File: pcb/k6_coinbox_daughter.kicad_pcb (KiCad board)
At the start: 2 copper layers, 45 x 35 mm, 17 parts, among them J1 COIN, J2 BTN_A, J3 BTN_B, J4 TO_ESP32, U1 PC817, U2 PC817, U3 PC817

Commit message: feat: update daughter board J4 to 6-pin header (separate +3V3 and +5V)
- J4 now has 6 pins matching carrier board J_COIN: COIN, A, B, 3V3, GND, 5V
- VCC_3V3 powers pull-up resistors R4/R5/R6 (3.3V logic for ESP32)
- VCC_5V available for optocoupler LED drive (input side)
- Pin order enables straight ribbon cable connection to carrier board
- Updated documentation and regenerated PCB file

Co-Authored-By: Devin AI <158243242+devin-ai-integration[bot]@users.noreply.github.com>
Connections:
- J4 pad 1: VCC -> COIN_SENSE
- J4 pad 2: COIN_SENSE -> BTN_A
- J4 pad 3: BTN_A -> BTN_B
- J4 pad 4: BTN_B -> VCC_3V3
- R4 pad 1: VCC -> VCC_3V3
- R5 pad 1: VCC -> VCC_3V3
- R6 pad 1: VCC -> VCC_3V3
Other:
- board text added: "3V3"
- board text added: "5V"
- board text removed: "VCC"
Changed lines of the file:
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@@
     )
     (net 0 "")
-(net 1 "VCC")
+(net 1 "VCC_3V3")
 (net 2 "GND")
 (net 3 "COIN_SENSE")
@@
 (net 13 "OPTO2_CA")
 (net 14 "OPTO3_CA")
+(net 15 "VCC_5V")
     (gr_line (start 131.5 90.0) (end 173.5 90.0) (stroke (width 0.05) (type default)) (layer "Edge.Cuts"))
 (gr_line (start 131.5 125.0) (end 173.5 125.0) (stroke (width 0.05) (type default)) (layer "Edge.Cuts"))
@@
   (fp_line (start -2.810 -1.0) (end 2.810 -1.0) (stroke (width 0.12) (type default)) (layer "F.SilkS"))
   (fp_line (start -2.810 1.0) (end 2.810 1.0) (stroke (width 0.12) (type default)) (layer "F.SilkS"))
-(pad "1" thru_hole circle (at -3.810 0.000) (size 1.7 1.7) (drill 1.0) (layers "*.Cu" "*.Mask") (net 1 "VCC"))
+(pad "1" thru_hole circle (at -3.810 0.000) (size 1.7 1.7) (drill 1.0) (layers "*.Cu" "*.Mask") (net 1 "VCC_3V3"))
 (pad "2" thru_hole circle (at 3.810 0.000) (size 1.7 1.7) (drill 1.0) (layers "*.Cu" "*.Mask") (net 3 "COIN_SENSE"))
 )
@@
   (fp_line (start -2.810 -1.0) (end 2.810 -1.0) (stroke (width 0.12) (type default)) (layer "F.SilkS"))
   (fp_line (start -2.810 1.0) (end 2.810 1.0) (stroke (width 0.12) (type default)) (layer "F.SilkS"))
-(pad "1" thru_hole circle (at -3.810 0.000) (size 1.7 1.7) (drill 1.0) (layers "*.Cu" "*.Mask") (net 1 "VCC"))
+(pad "1" thru_hole circle (at -3.810 0.000) (size 1.7 1.7) (drill 1.0) (layers "*.Cu" "*.Mask") (net 1 "VCC_3V3"))
 (pad "2" thru_hole circle (at 3.810 0.000) (size 1.7 1.7) (drill 1.0) (layers "*.Cu" "*.Mask") (net 4 "BTN_A"))
 )
@@
   (fp_line (start -2.810 -1.0) (end 2.810 -1.0) (stroke (width 0.12) (type default)) (layer "F.SilkS"))
   (fp_line (start -2.810 1.0) (end 2.810 1.0) (stroke (width 0.12) (type default)) (layer "F.SilkS"))
-(pad "1" thru_hole circle (at -3.810 0.000) (size 1.7 1.7) (drill 1.0) (layers "*.Cu" "*.Mask") (net 1 "VCC"))
+(pad "1" thru_hole circle (at -3.810 0.000) (size 1.7 1.7) (drill 1.0) (layers "*.Cu" "*.Mask") (net 1 "VCC_3V3"))
 (pad "2" thru_hole circle (at 3.810 0.000) (size 1.7 1.7) (drill 1.0) (layers "*.Cu" "*.Mask") (net 5 "BTN_B"))
 )
@@
   (effects (font (size 0.8 0.8) (thickness 0.12)))
 )
-  (fp_rect (start -1.5 -6.850) (end 1.5 6.850) (stroke (width 0.05) (type default)) (fill none) (layer "F.CrtYd"))
-(pad "1" thru_hole circle (at 0.000 -5.080) (size 1.7 1.7) (drill 1.0) (layers "*.Cu" "*.Mask") (net 1 "VCC"))
-(pad "2" thru_hole circle (at 0.000 -2.540) (size 1.7 1.7) (drill 1.0) (layers "*.Cu" "*.Mask") (net 3 "COIN_SENSE"))
-(pad "3" thru_hole circle (at 0.000 0.000) (size 1.7 1.7) (drill 1.0) (layers "*.Cu" "*.Mask") (net 4 "BTN_A"))
-(pad "4" thru_hole circle (at 0.000 2.540) (size 1.7 1.7) (drill 1.0) (layers "*.Cu" "*.Mask") (net 5 "BTN_B"))
-(pad "5" thru_hole circle (at 0.000 5.080) (size 1.7 1.7) (drill 1.0) (layers "*.Cu" "*.Mask") (net 2 "GND"))
+  (fp_rect (start -1.5 -8.120) (end 1.5 8.120) (stroke (width 0.05) (type default)) (fill none) (layer "F.CrtYd"))
+(pad "1" thru_hole circle (at 0.000 -6.350) (size 1.7 1.7) (drill 1.0) (layers "*.Cu" "*.Mask") (net 3 "COIN_SENSE"))
+(pad "2" thru_hole circle (at 0.000 -3.810) (size 1.7 1.7) (drill 1.0) (layers "*.Cu" "*.Mask") (net 4 "BTN_A"))
+(pad "3" thru_hole circle (at 0.000 -1.270) (size 1.7 1.7) (drill 1.0) (layers "*.Cu" "*.Mask") (net 5 "BTN_B"))
+(pad "4" thru_hole circle (at 0.000 1.270) (size 1.7 1.7) (drill 1.0) (layers "*.Cu" "*.Mask") (net 1 "VCC_3V3"))
+(pad "5" thru_hole circle (at 0.000 3.810) (size 1.7 1.7) (drill 1.0) (layers "*.Cu" "*.Mask") (net 2 "GND"))
+(pad "6" thru_hole circle (at 0.000 6.350) (size 1.7 1.7) (drill 1.0) (layers "*.Cu" "*.Mask") (net 15 "VCC_5V"))
 )
 (footprint "K6_COINBOX:MH1" (layer "F.Cu")
@@
   (effects (font (size 0.8 0.8) (thickness 0.12)))
 )
-(gr_text "VCC" (at 172.000 98.500) (layer "F.SilkS")
-  (effects (font (size 0.8 0.8) (thickness 0.12)))
-)
-(gr_text "COIN" (at 172.000 101.000) (layer "F.SilkS")
-  (effects (font (size 0.8 0.8) (thickness 0.12)))
-)
-(gr_text "A" (at 172.000 103.500) (layer "F.SilkS")
-  (effects (font (size 0.8 0.8) (thickness 0.12)))
-)
-(gr_text "B" (at 172.000 106.000) (layer "F.SilkS")
-  (effects (font (size 0.8 0.8) (thickness 0.12)))
-)
-(gr_text "GND" (at 172.000 108.500) (layer "F.SilkS")
-  (effects (font (size 0.8 0.8) (thickness 0.12)))
-)
+(gr_text "COIN" (at 172.000 98.000) (layer "F.SilkS")
+  (effects (font (size 0.8 0.8) (thickness 0.12)))
+)
+(gr_text "A" (at 172.000 100.500) (layer "F.SilkS")
+  (effects (font (size 0.8 0.8) (thickness 0.12)))
+)
+(gr_text "B" (at 172.000 103.000) (layer "F.SilkS")
+  (effects (font (size 0.8 0.8) (thickness 0.12)))
+)
+(gr_text "3V3" (at 172.000 105.500) (layer "F.SilkS")
+  (effects (font (size 0.8 0.8) (thickness 0.12)))
+)
+(gr_text "GND" (at 172.000 108.000) (layer "F.SilkS")
+  (effects (font (size 0.8 0.8) (thickness 0.12)))
+)
+(gr_text "5V" (at 172.000 110.500) (layer "F.SilkS")
+  (effects (font (size 0.8 0.8) (thickness 0.12)))
+)

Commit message: feat: integrate VCC_5V into daughter board input circuit
- VCC_5V now drives pin 1 of each screw terminal (C+/A+/B+)
- A+B box contacts are dry switches bridging pin 1 to pin 2
- When switch closes: 5V -> R(470R) -> opto LED -> GND = 8mA
- Opto LED cathodes now connected to GND (were floating to return pin)
- No external voltage source needed for the A+B box contacts
- Updated circuit diagram and wiring documentation

Co-Authored-By: Devin AI <158243242+devin-ai-integration[bot]@users.noreply.github.com>
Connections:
- J1 pad 1: COIN_IN_A -> VCC_5V
- J2 pad 1: BTNA_IN_A -> VCC_5V
- J3 pad 1: BTNB_IN_A -> VCC_5V
- R1 pad 1: COIN_IN_A -> COIN_IN_B
- R2 pad 1: BTNA_IN_A -> BTNA_IN_B
- R3 pad 1: BTNB_IN_A -> BTNB_IN_B
- U1 pad 2: COIN_IN_B -> GND
- U2 pad 2: BTNA_IN_B -> GND
- U3 pad 2: BTNB_IN_B -> GND
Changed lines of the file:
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@@
   (effects (font (size 0.8 0.8) (thickness 0.12)))
 )
-(pad "1" thru_hole circle (at -2.540 0.000) (size 2.5 2.5) (drill 1.3) (layers "*.Cu" "*.Mask") (net 6 "COIN_IN_A"))
+(pad "1" thru_hole circle (at -2.540 0.000) (size 2.5 2.5) (drill 1.3) (layers "*.Cu" "*.Mask") (net 15 "VCC_5V"))
 (pad "2" thru_hole circle (at 2.540 0.000) (size 2.5 2.5) (drill 1.3) (layers "*.Cu" "*.Mask") (net 7 "COIN_IN_B"))
 )
@@
   (effects (font (size 0.8 0.8) (thickness 0.12)))
 )
-(pad "1" thru_hole circle (at -2.540 0.000) (size 2.5 2.5) (drill 1.3) (layers "*.Cu" "*.Mask") (net 8 "BTNA_IN_A"))
+(pad "1" thru_hole circle (at -2.540 0.000) (size 2.5 2.5) (drill 1.3) (layers "*.Cu" "*.Mask") (net 15 "VCC_5V"))
 (pad "2" thru_hole circle (at 2.540 0.000) (size 2.5 2.5) (drill 1.3) (layers "*.Cu" "*.Mask") (net 9 "BTNA_IN_B"))
 )
@@
   (effects (font (size 0.8 0.8) (thickness 0.12)))
 )
-(pad "1" thru_hole circle (at -2.540 0.000) (size 2.5 2.5) (drill 1.3) (layers "*.Cu" "*.Mask") (net 10 "BTNB_IN_A"))
+(pad "1" thru_hole circle (at -2.540 0.000) (size 2.5 2.5) (drill 1.3) (layers "*.Cu" "*.Mask") (net 15 "VCC_5V"))
 (pad "2" thru_hole circle (at 2.540 0.000) (size 2.5 2.5) (drill 1.3) (layers "*.Cu" "*.Mask") (net 11 "BTNB_IN_B"))
 )
@@
   (fp_line (start -2.810 -1.0) (end 2.810 -1.0) (stroke (width 0.12) (type default)) (layer "F.SilkS"))
   (fp_line (start -2.810 1.0) (end 2.810 1.0) (stroke (width 0.12) (type default)) (layer "F.SilkS"))
-(pad "1" thru_hole circle (at -3.810 0.000) (size 1.7 1.7) (drill 1.0) (layers "*.Cu" "*.Mask") (net 6 "COIN_IN_A"))
+(pad "1" thru_hole circle (at -3.810 0.000) (size 1.7 1.7) (drill 1.0) (layers "*.Cu" "*.Mask") (net 7 "COIN_IN_B"))
 (pad "2" thru_hole circle (at 3.810 0.000) (size 1.7 1.7) (drill 1.0) (layers "*.Cu" "*.Mask") (net 12 "OPTO1_CA"))
 )
@@
   (fp_line (start -2.810 -1.0) (end 2.810 -1.0) (stroke (width 0.12) (type default)) (layer "F.SilkS"))
   (fp_line (start -2.810 1.0) (end 2.810 1.0) (stroke (width 0.12) (type default)) (layer "F.SilkS"))
-(pad "1" thru_hole circle (at -3.810 0.000) (size 1.7 1.7) (drill 1.0) (layers "*.Cu" "*.Mask") (net 8 "BTNA_IN_A"))
+(pad "1" thru_hole circle (at -3.810 0.000) (size 1.7 1.7) (drill 1.0) (layers "*.Cu" "*.Mask") (net 9 "BTNA_IN_B"))
 (pad "2" thru_hole circle (at 3.810 0.000) (size 1.7 1.7) (drill 1.0) (layers "*.Cu" "*.Mask") (net 13 "OPTO2_CA"))
 )
@@
   (fp_line (start -2.810 -1.0) (end 2.810 -1.0) (stroke (width 0.12) (type default)) (layer "F.SilkS"))
   (fp_line (start -2.810 1.0) (end 2.810 1.0) (stroke (width 0.12) (type default)) (layer "F.SilkS"))
-(pad "1" thru_hole circle (at -3.810 0.000) (size 1.7 1.7) (drill 1.0) (layers "*.Cu" "*.Mask") (net 10 "BTNB_IN_A"))
+(pad "1" thru_hole circle (at -3.810 0.000) (size 1.7 1.7) (drill 1.0) (layers "*.Cu" "*.Mask") (net 11 "BTNB_IN_B"))
 (pad "2" thru_hole circle (at 3.810 0.000) (size 1.7 1.7) (drill 1.0) (layers "*.Cu" "*.Mask") (net 14 "OPTO3_CA"))
 )
@@
   (fp_circle (center -4.310 -1.270) (end -4.010 -1.270) (stroke (width 0.12) (type default)) (fill solid) (layer "F.SilkS"))
 (pad "1" thru_hole circle (at -3.810 -1.270) (size 1.6 1.6) (drill 0.8) (layers "*.Cu" "*.Mask") (net 12 "OPTO1_CA"))
-(pad "2" thru_hole circle (at -3.810 1.270) (size 1.6 1.6) (drill 0.8) (layers "*.Cu" "*.Mask") (net 7 "COIN_IN_B"))
+(pad "2" thru_hole circle (at -3.810 1.270) (size 1.6 1.6) (drill 0.8) (layers "*.Cu" "*.Mask") (net 2 "GND"))
 (pad "4" thru_hole circle (at 3.810 -1.270) (size 1.6 1.6) (drill 0.8) (layers "*.Cu" "*.Mask") (net 3 "COIN_SENSE"))
 (pad "3" thru_hole circle (at 3.810 1.270) (size 1.6 1.6) (drill 0.8) (layers "*.Cu" "*.Mask") (net 2 "GND"))
@@
   (fp_circle (center -4.310 -1.270) (end -4.010 -1.270) (stroke (width 0.12) (type default)) (fill solid) (layer "F.SilkS"))
 (pad "1" thru_hole circle (at -3.810 -1.270) (size 1.6 1.6) (drill 0.8) (layers "*.Cu" "*.Mask") (net 13 "OPTO2_CA"))
-(pad "2" thru_hole circle (at -3.810 1.270) (size 1.6 1.6) (drill 0.8) (layers "*.Cu" "*.Mask") (net 9 "BTNA_IN_B"))
+(pad "2" thru_hole circle (at -3.810 1.270) (size 1.6 1.6) (drill 0.8) (layers "*.Cu" "*.Mask") (net 2 "GND"))
 (pad "4" thru_hole circle (at 3.810 -1.270) (size 1.6 1.6) (drill 0.8) (layers "*.Cu" "*.Mask") (net 4 "BTN_A"))
 (pad "3" thru_hole circle (at 3.810 1.270) (size 1.6 1.6) (drill 0.8) (layers "*.Cu" "*.Mask") (net 2 "GND"))
@@
   (fp_circle (center -4.310 -1.270) (end -4.010 -1.270) (stroke (width 0.12) (type default)) (fill solid) (layer "F.SilkS"))
 (pad "1" thru_hole circle (at -3.810 -1.270) (size 1.6 1.6) (drill 0.8) (layers "*.Cu" "*.Mask") (net 14 "OPTO3_CA"))
-(pad "2" thru_hole circle (at -3.810 1.270) (size 1.6 1.6) (drill 0.8) (layers "*.Cu" "*.Mask") (net 11 "BTNB_IN_B"))
+(pad "2" thru_hole circle (at -3.810 1.270) (size 1.6 1.6) (drill 0.8) (layers "*.Cu" "*.Mask") (net 2 "GND"))
 (pad "4" thru_hole circle (at 3.810 -1.270) (size 1.6 1.6) (drill 0.8) (layers "*.Cu" "*.Mask") (net 5 "BTN_B"))
 (pad "3" thru_hole circle (at 3.810 1.270) (size 1.6 1.6) (drill 0.8) (layers "*.Cu" "*.Mask") (net 2 "GND"))

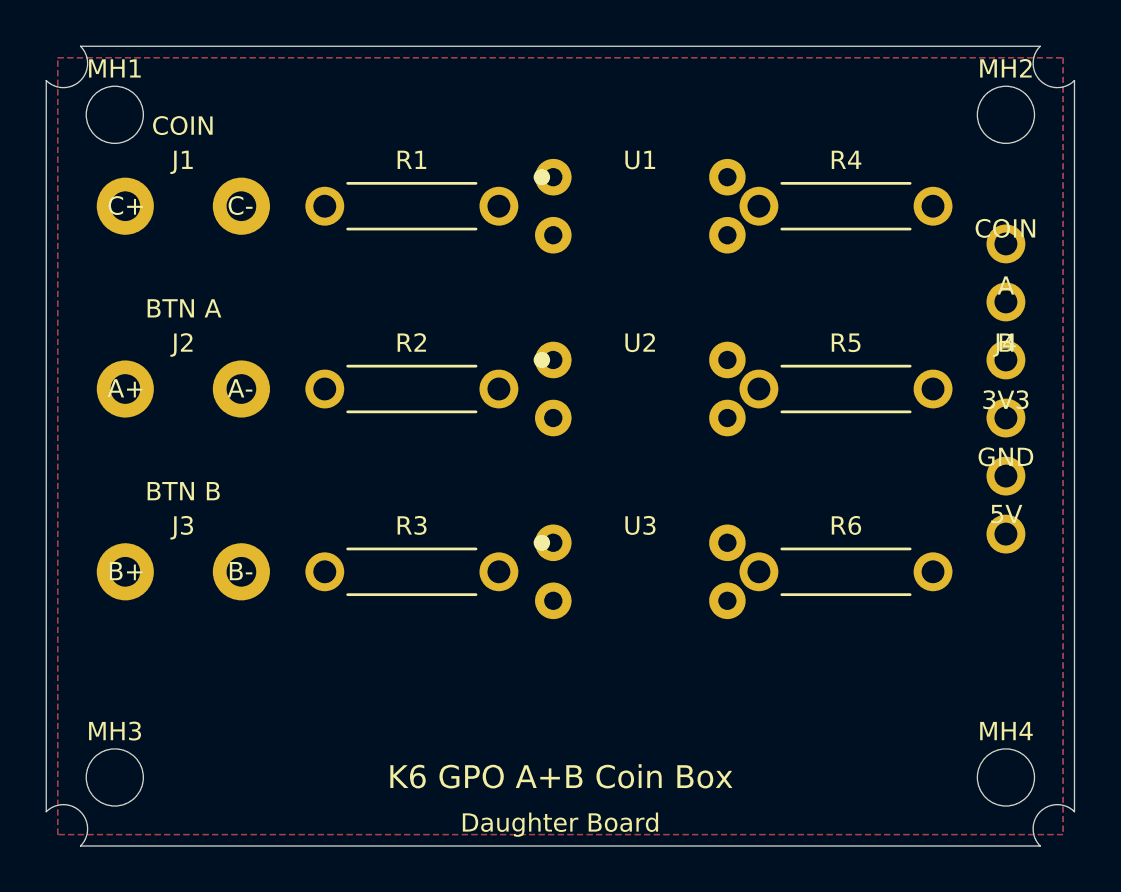
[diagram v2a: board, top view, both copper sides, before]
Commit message: pcb: replace with routed board files, remove pre-generated gerbers
- Carrier board: replaced with user's routed k6_carrier_rev2 PCB
- Daughter board: replaced with user's routed k6_coinbox_daughter PCB
- Removed pcb/gerbers/ directory (users should export their own
  gerbers from KiCad with their preferred fabricator settings)
- Updated docs to reference KiCad export instead of pre-generated files

Co-Authored-By: Devin AI <158243242+devin-ai-integration[bot]@users.noreply.github.com>
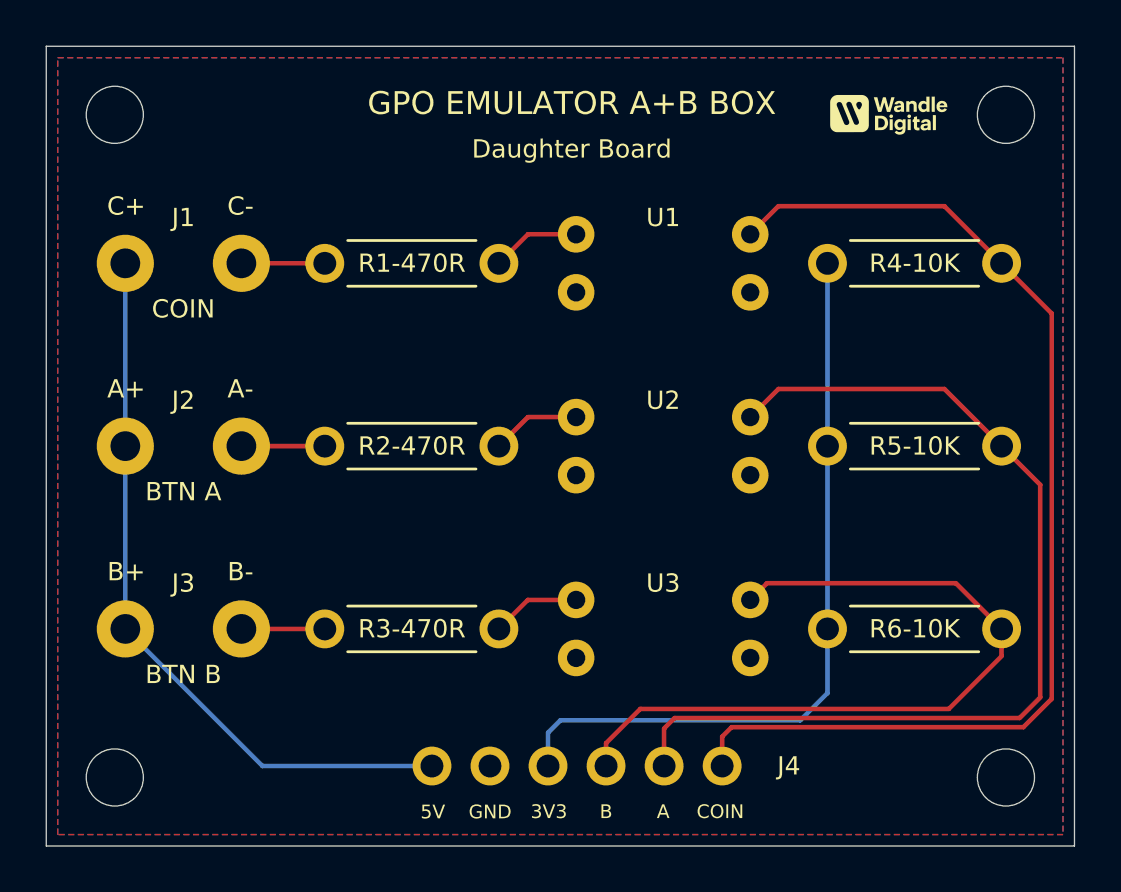
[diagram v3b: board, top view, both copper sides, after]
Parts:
- moved J4 25.0 mm to (153.2, 121.5), turned to -90 degrees
- moved R4-10K 3.91 mm to (168.0, 99.5)
- moved R5-10K 3.91 mm to (168.0, 107.5)
- moved R6-10K 3.91 mm to (168.0, 115.5)
- moved U1 2.69 mm to (157.0, 99.5)
- moved U2 2.69 mm to (157.0, 107.5)
- moved U3 2.69 mm to (157.0, 115.5)
- moved J1 2.50 mm to (136.0, 99.5)
- moved J2 2.50 mm to (136.0, 107.5)
- moved J3 2.50 mm to (136.0, 115.5)
- moved R1-470R 2.50 mm to (146.0, 99.5)
- moved R2-470R 2.50 mm to (146.0, 107.5)
- moved R3-470R 2.50 mm to (146.0, 115.5)
- renumbered R1 to R1-470R, R2 to R2-470R, R3 to R3-470R, R4 to R4-10K, R5 to R5-10K, R6 to R6-10K
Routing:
- net COIN_SENSE: track 0.00 -> 48.9 mm
- net BTN_A: track 0.00 -> 42.9 mm
- net VCC_3V3: track 0.00 -> 33.2 mm
- net BTN_B: track 0.00 -> 33.2 mm
- net VCC_5V: track 0.00 -> 31.9 mm
- net OPTO3_CA: track 0.00 -> 3.91 mm
- net OPTO2_CA: track 0.00 -> 3.91 mm
- net OPTO1_CA: track 0.00 -> 3.91 mm
- net COIN_IN_B: track 0.00 -> 3.65 mm
- net BTNB_IN_B: track 0.00 -> 3.65 mm
- net BTNA_IN_B: track 0.00 -> 3.65 mm
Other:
- outline, holes or cut-outs redrawn
- board text added: "GPO EMULATOR A+B BOX"
- board text removed: "K6 GPO A+B Coin Box"
